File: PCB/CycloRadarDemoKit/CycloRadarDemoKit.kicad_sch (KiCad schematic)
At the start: 13 parts, among them J101 I2C conn, J102 CAN, J103 100BASE-T1, J104 Radar debug, J105 Radar pins, U101 RADAR POGO pins

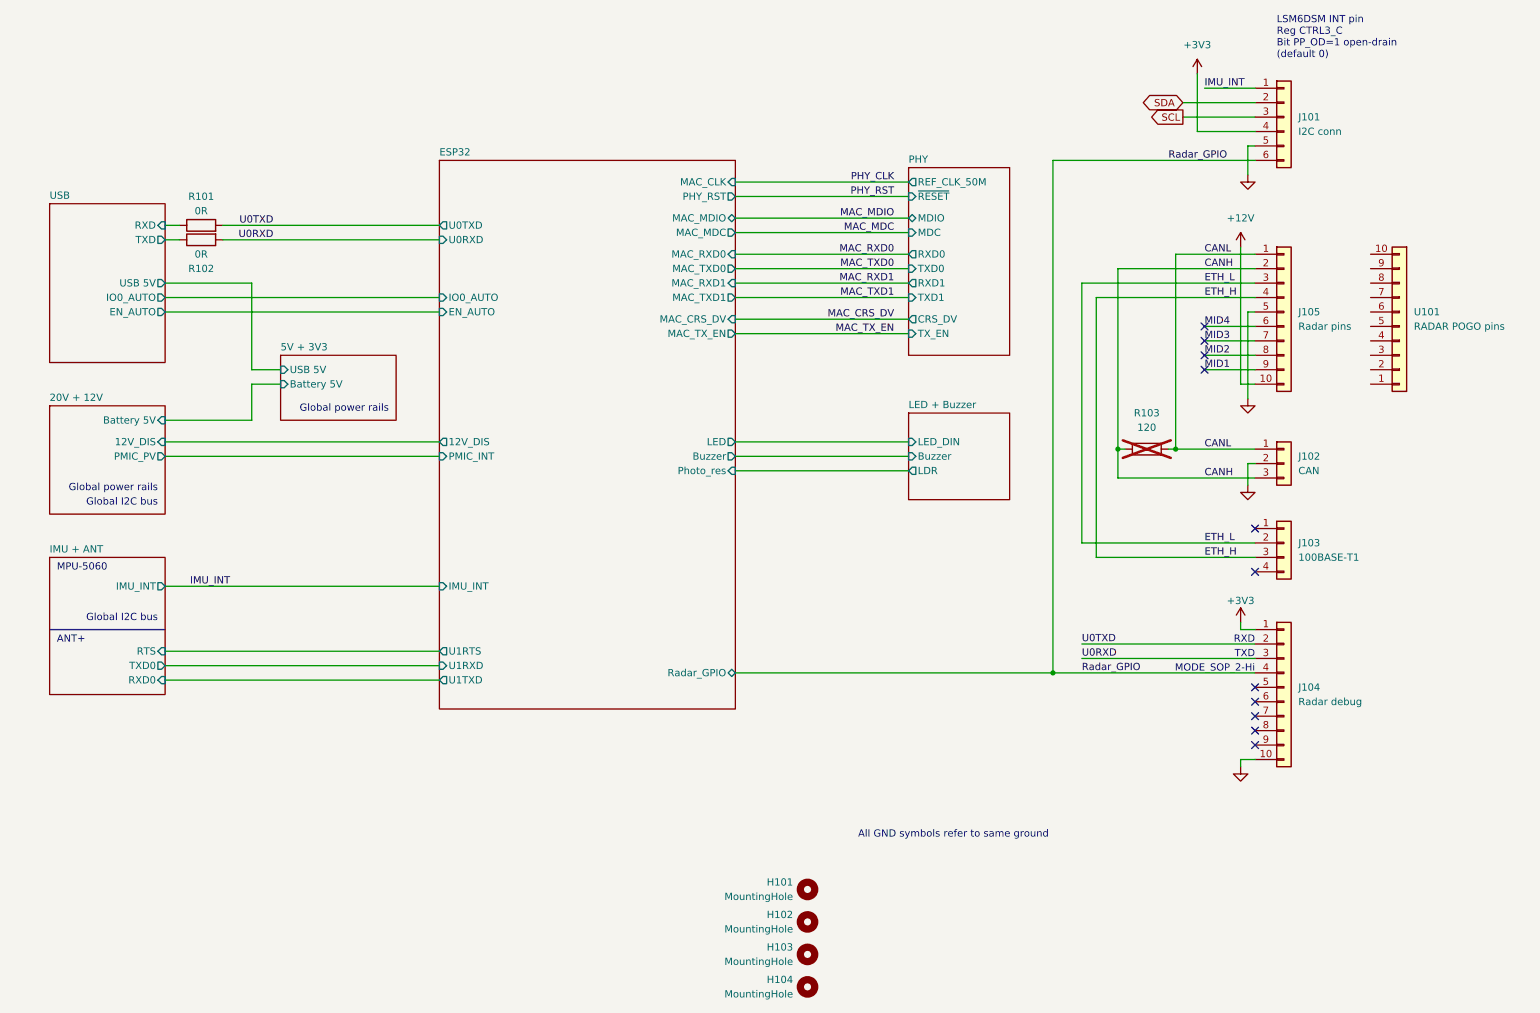
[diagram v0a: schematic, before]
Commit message: reanotated schematic, routing started
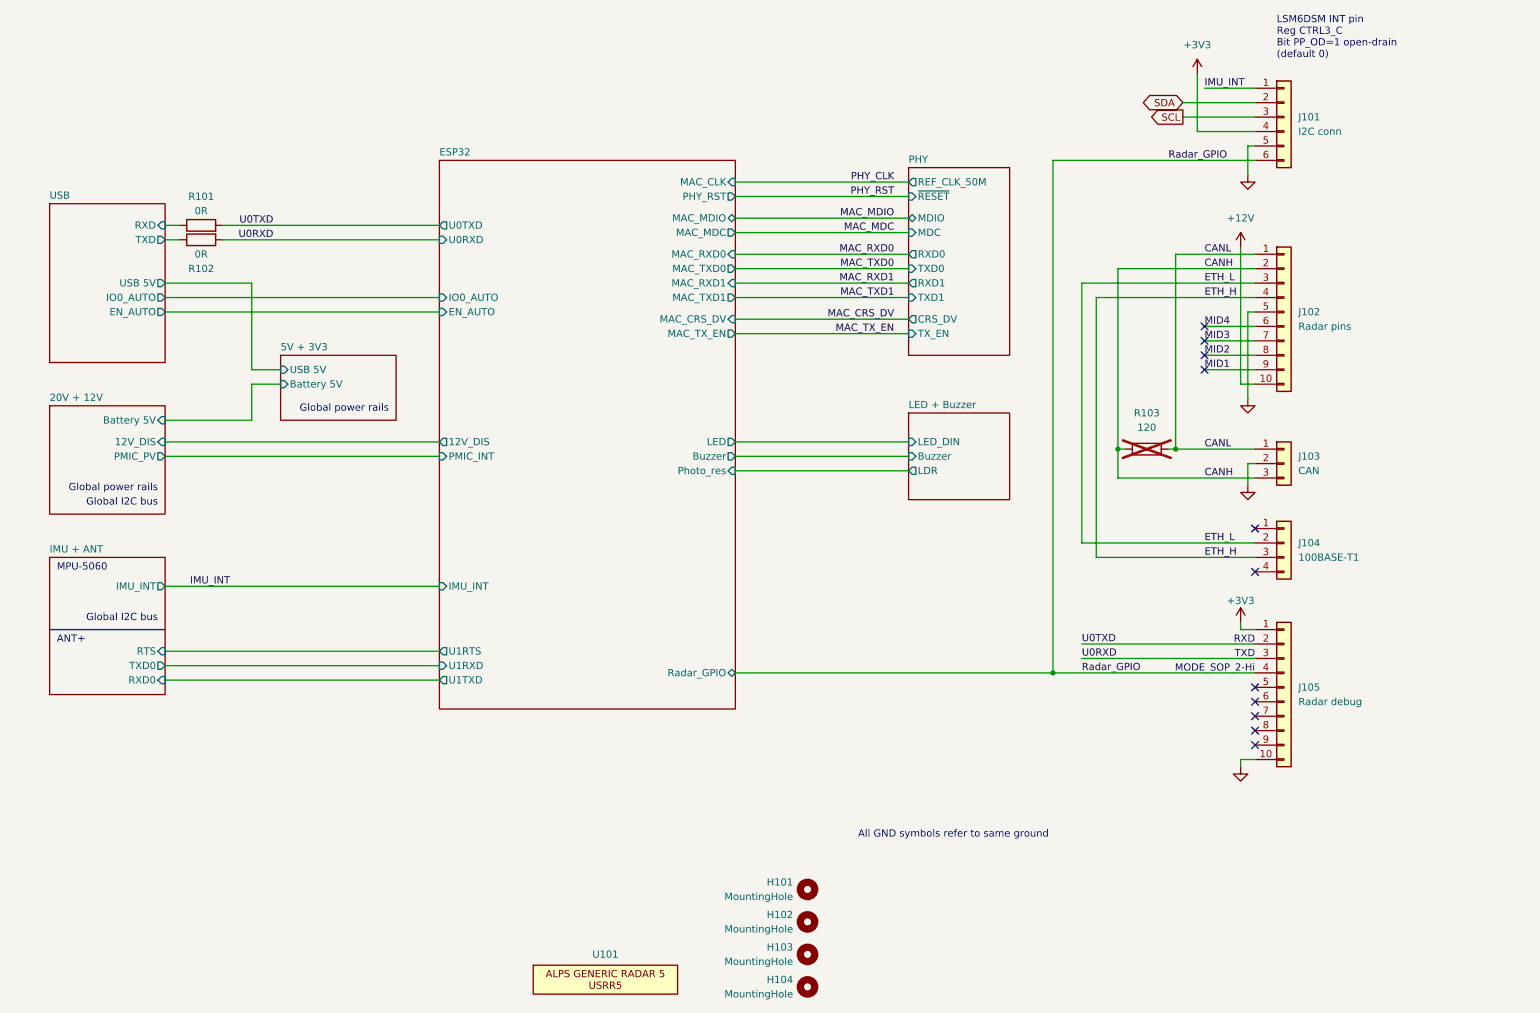
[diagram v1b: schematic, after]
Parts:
- removed U101: RADAR POGO pins, alps_modules:ALPS_USRR5, symbol alps_modules:ALPS_Generic_Radar_5
- added U101: ~, alps_modules:ALPS_USRR5_woPins, symbol alps_modules:ALPS_Generic_Radar_5_block
- renumbered J105 to J102, J102 to J103, J103 to J104, J104 to J105
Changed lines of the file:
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@@
   (symbol (lib_id "Connector_Generic:Conn_01x03") (at 251.46 97.79 0) (unit 1)
     (in_bom yes) (on_board yes) (dnp no) (fields_autoplaced)
-    (property "Reference" "J102" (at 254 96.52 0)
+    (property "Reference" "J103" (at 254 96.52 0)
       (effects (font (size 1.27 1.27)) (justify left))
     )
@@
       (project "CycloRadarDemoKit"
         (path "/c2cd7ca4-4652-4b3d-a3a8-1cfa66cb11e9"
-          (reference "J102") (unit 1)
+          (reference "J103") (unit 1)
         )
       )
@@
   (symbol (lib_id "Connector_Generic:Conn_01x10") (at 251.46 71.12 0) (unit 1)
     (in_bom yes) (on_board yes) (dnp no) (fields_autoplaced)
-    (property "Reference" "J105" (at 254 71.12 0)
+    (property "Reference" "J102" (at 254 71.12 0)
       (effects (font (size 1.27 1.27)) (justify left))
     )
@@
       (project "CycloRadarDemoKit"
         (path "/c2cd7ca4-4652-4b3d-a3a8-1cfa66cb11e9"
-          (reference "J105") (unit 1)
+          (reference "J102") (unit 1)
         )
       )
@@
   (symbol (lib_id "power:GND") (at 245.11 101.6 0) (unit 1)
     (in_bom yes) (on_board yes) (dnp no) (fields_autoplaced)
-    (property "Reference" "#PWR0107" (at 245.11 107.95 0)
+    (property "Reference" "#PWR0105" (at 245.11 107.95 0)
       (effects (font (size 1.27 1.27)) hide)
     )
@@
       (project "CycloRadarDemoKit"
         (path "/c2cd7ca4-4652-4b3d-a3a8-1cfa66cb11e9"
-          (reference "#PWR0107") (unit 1)
-        )
-      )
-    )
-  )
-  (symbol (lib_id "alps_modules:ALPS_Generic_Radar_5") (at 271.78 72.39 180) (unit 1)
-    (in_bom yes) (on_board yes) (dnp no) (fields_autoplaced)
-    (property "Reference" "U101" (at 274.32 71.12 0)
-      (effects (font (size 1.27 1.27)) (justify right))
-    )
-    (property "Value" "RADAR POGO pins" (at 274.32 73.66 0)
-      (effects (font (size 1.27 1.27)) (justify right))
-    )
-    (property "Footprint" "alps_modules:ALPS_USRR5" (at 271.78 72.39 0)
-      (effects (font (size 1.27 1.27)) hide)
-    )
-    (property "Datasheet" "" (at 271.78 72.39 0)
-      (effects (font (size 1.27 1.27)) hide)
-    )
-    (pin "3")
-    (pin "8")
-    (pin "6")
-    (pin "10")
-    (pin "4")
-    (pin "7")
-    (pin "5")
-    (pin "1")
-    (pin "2")
-    (pin "9")
-    (instances
-      (project "CycloRadarDemoKit"
-        (path "/c2cd7ca4-4652-4b3d-a3a8-1cfa66cb11e9"
-          (reference "U101") (unit 1)
+          (reference "#PWR0105") (unit 1)
         )
       )
@@
   (symbol (lib_id "power:+3V3") (at 243.84 125.73 0) (unit 1)
     (in_bom yes) (on_board yes) (dnp no)
-    (property "Reference" "#PWR0105" (at 243.84 129.54 0)
+    (property "Reference" "#PWR0106" (at 243.84 129.54 0)
       (effects (font (size 1.27 1.27)) hide)
     )
@@
       (project "CycloRadarDemoKit"
         (path "/c2cd7ca4-4652-4b3d-a3a8-1cfa66cb11e9"
-          (reference "#PWR0105") (unit 1)
+          (reference "#PWR0106") (unit 1)
         )
       )
@@
   (symbol (lib_id "power:GND") (at 243.84 151.13 0) (unit 1)
     (in_bom yes) (on_board yes) (dnp no) (fields_autoplaced)
-    (property "Reference" "#PWR0106" (at 243.84 157.48 0)
+    (property "Reference" "#PWR0107" (at 243.84 157.48 0)
       (effects (font (size 1.27 1.27)) hide)
     )
@@
       (project "CycloRadarDemoKit"
         (path "/c2cd7ca4-4652-4b3d-a3a8-1cfa66cb11e9"
-          (reference "#PWR0106") (unit 1)
+          (reference "#PWR0107") (unit 1)
+        )
+      )
+    )
+  )
+  (symbol (lib_id "alps_modules:ALPS_Generic_Radar_5_block") (at 132.08 184.785 0) (unit 1)
+    (in_bom yes) (on_board yes) (dnp no) (fields_autoplaced)
+    (property "Reference" "U101" (at 132.08 184.15 0)
+      (effects (font (size 1.27 1.27)))
+    )
+    (property "Value" "~" (at 132.08 184.785 0)
+      (effects (font (size 1.27 1.27)))
+    )
+    (property "Footprint" "alps_modules:ALPS_USRR5_woPins" (at 132.08 184.785 0)
+      (effects (font (size 1.27 1.27)) hide)
+    )
+    (property "Datasheet" "" (at 132.08 184.785 0)
+      (effects (font (size 1.27 1.27)) hide)
+    )
+    (instances
+      (project "CycloRadarDemoKit"
+        (path "/c2cd7ca4-4652-4b3d-a3a8-1cfa66cb11e9"
+          (reference "U101") (unit 1)
         )
       )
@@
     )
   )
-  (symbol (lib_id "Connector_Generic:Conn_01x10") (at 251.46 137.16 0) (unit 1)
-    (in_bom yes) (on_board yes) (dnp no) (fields_autoplaced)
-    (property "Reference" "J104" (at 254 137.16 0)
+  (symbol (lib_name "Conn_01x10_1") (lib_id "Connector_Generic:Conn_01x10") (at 251.46 137.16 0) (unit 1)
+    (in_bom yes) (on_board yes) (dnp no) (fields_autoplaced)
+    (property "Reference" "J105" (at 254 137.16 0)
       (effects (font (size 1.27 1.27)) (justify left))
     )
@@
     (pin "6")
     (pin "1")
-    (instances
-      (project "CycloRadarDemoKit"
-        (path "/c2cd7ca4-4652-4b3d-a3a8-1cfa66cb11e9"
-          (reference "J104") (unit 1)
+    (pin "NC")
+    (instances
+      (project "CycloRadarDemoKit"
+        (path "/c2cd7ca4-4652-4b3d-a3a8-1cfa66cb11e9"
+          (reference "J105") (unit 1)
         )
       )
@@
   (symbol (lib_id "Connector_Generic:Conn_01x04") (at 251.46 111.76 0) (unit 1)
     (in_bom yes) (on_board yes) (dnp no) (fields_autoplaced)
-    (property "Reference" "J103" (at 254 111.76 0)
+    (property "Reference" "J104" (at 254 111.76 0)
       (effects (font (size 1.27 1.27)) (justify left))
     )
@@
       (project "CycloRadarDemoKit"
         (path "/c2cd7ca4-4652-4b3d-a3a8-1cfa66cb11e9"
-          (reference "J103") (unit 1)
-        )
-      )
+          (reference "J104") (unit 1)
+        )
+      )

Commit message: silkscreen repaired
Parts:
- H101, H102, H103, H104: footprint MountingHole:MountingHole_2.7mm_M2.5_ISO7380 -> MountingHole:MountingHole_2.7mm_M2.5_ISO7380_Pad
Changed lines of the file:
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@@
       (effects (font (size 1.27 1.27)) (justify left))
     )
-    (property "Footprint" "MountingHole:MountingHole_2.7mm_M2.5_ISO7380" (at 167.64 178.435 0)
+    (property "Footprint" "MountingHole:MountingHole_2.7mm_M2.5_ISO7380_Pad" (at 167.64 178.435 0)
       (effects (font (size 1.27 1.27)) hide)
     )
@@
       (effects (font (size 1.27 1.27)) (justify left))
     )
-    (property "Footprint" "MountingHole:MountingHole_2.7mm_M2.5_ISO7380" (at 167.64 172.72 0)
+    (property "Footprint" "MountingHole:MountingHole_2.7mm_M2.5_ISO7380_Pad" (at 167.64 172.72 0)
       (effects (font (size 1.27 1.27)) hide)
     )
@@
       (effects (font (size 1.27 1.27)) (justify left))
     )
-    (property "Footprint" "MountingHole:MountingHole_2.7mm_M2.5_ISO7380" (at 167.64 184.15 0)
+    (property "Footprint" "MountingHole:MountingHole_2.7mm_M2.5_ISO7380_Pad" (at 167.64 184.15 0)
       (effects (font (size 1.27 1.27)) hide)
     )
@@
       (effects (font (size 1.27 1.27)) (justify left))
     )
-    (property "Footprint" "MountingHole:MountingHole_2.7mm_M2.5_ISO7380" (at 167.64 189.865 0)
-      (effects (font (size 1.27 1.27)) hide)
-    )
+    (property "Footprint" "MountingHole:MountingHole_2.7mm_M2.5_ISO7380_Pad" (at 167.64 189.865 0)
+      (effects (font (size 1.27 1.27)) hide)
+    )

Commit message: start of repair after review
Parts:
- J102, R103, U101: now left out of the parts list
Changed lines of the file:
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@@
+    (stroke (width 0) (type default))
+  )
+  (wire (pts (xy 218.44 114.3) (xy 246.38 114.3))
     (stroke (width 0) (type default))
   )
@@
     (stroke (width 0) (type default))
   )
-  (wire (pts (xy 215.9 111.76) (xy 246.38 111.76))
-    (stroke (width 0) (type default))
-  )
   (wire (pts (xy 243.84 127) (xy 243.84 125.73))
     (stroke (width 0) (type default))
@@
     (stroke (width 0) (type default))
   )
-  (wire (pts (xy 218.44 114.3) (xy 218.44 68.58))
-    (stroke (width 0) (type default))
-  )
   (wire (pts (xy 233.68 34.29) (xy 246.38 34.29))
     (stroke (width 0) (type default))
@@
     (stroke (width 0) (type default))
   )
-  (wire (pts (xy 215.9 111.76) (xy 215.9 66.04))
+  (wire (pts (xy 215.9 66.04) (xy 215.9 111.76))
     (stroke (width 0) (type default))
   )
@@
   )
   (wire (pts (xy 69.85 83.82) (xy 74.93 83.82))
+    (stroke (width 0) (type default))
+  )
+  (wire (pts (xy 218.44 68.58) (xy 218.44 114.3))
     (stroke (width 0) (type default))
   )
@@
     (stroke (width 0) (type default))
   )
+  (wire (pts (xy 246.38 111.76) (xy 215.9 111.76))
+    (stroke (width 0) (type default))
+  )
   (wire (pts (xy 237.49 76.2) (xy 246.38 76.2))
     (stroke (width 0) (type default))
@@
   )
   (wire (pts (xy 54.61 130.81) (xy 102.87 130.81))
-    (stroke (width 0) (type default))
-  )
-  (wire (pts (xy 218.44 114.3) (xy 246.38 114.3))
     (stroke (width 0) (type default))
   )
@@
   )
   (symbol (lib_id "Connector_Generic:Conn_01x10") (at 251.46 71.12 0) (unit 1)
-    (in_bom yes) (on_board yes) (dnp no) (fields_autoplaced)
+    (in_bom no) (on_board yes) (dnp no) (fields_autoplaced)
     (property "Reference" "J102" (at 254 71.12 0)
       (effects (font (size 1.27 1.27)) (justify left))
@@
   )
   (symbol (lib_id "alps_modules:ALPS_Generic_Radar_5_block") (at 132.08 184.785 0) (unit 1)
-    (in_bom yes) (on_board yes) (dnp no) (fields_autoplaced)
+    (in_bom no) (on_board yes) (dnp no) (fields_autoplaced)
     (property "Reference" "U101" (at 132.08 184.15 0)
       (effects (font (size 1.27 1.27)))
@@
   )
   (symbol (lib_id "Device:R") (at 227.33 95.25 90) (unit 1)
-    (in_bom yes) (on_board yes) (dnp yes) (fields_autoplaced)
+    (in_bom no) (on_board yes) (dnp yes) (fields_autoplaced)
     (property "Reference" "R103" (at 227.33 88.9 90)
       (effects (font (size 1.27 1.27)))

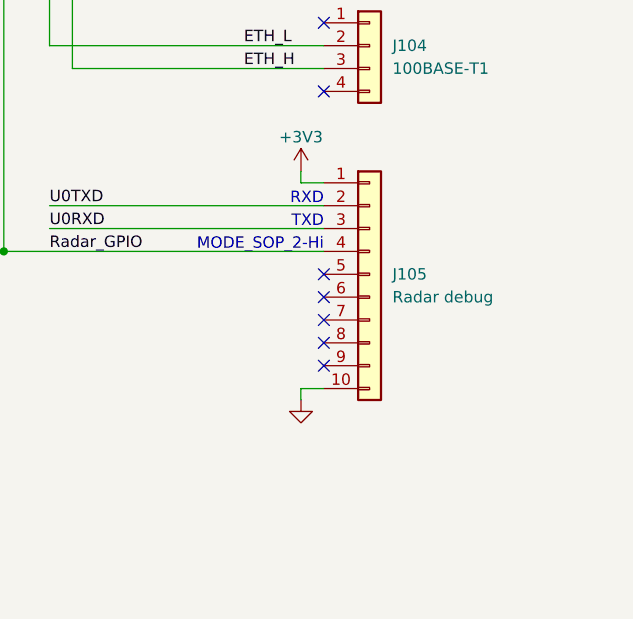
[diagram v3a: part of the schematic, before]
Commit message: Review changes WIP, USB ESD changed, MDIC pullup added
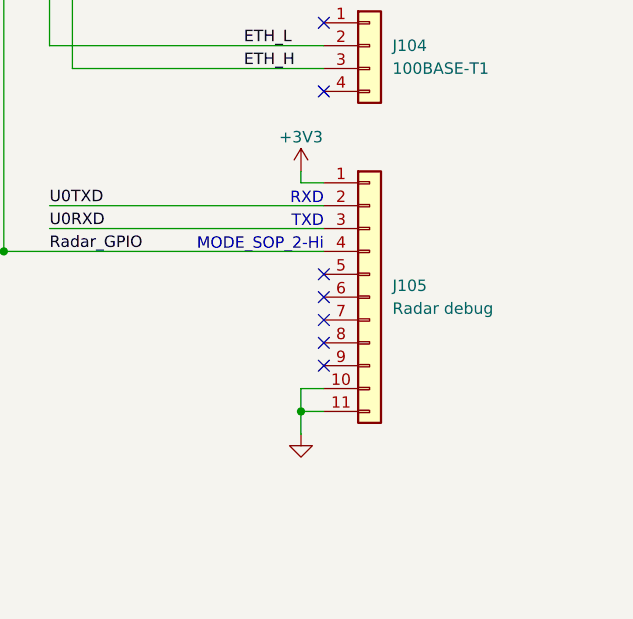
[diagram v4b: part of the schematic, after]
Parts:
- J105: symbol Connector_Generic:Conn_01x10 -> Connector_Generic:Conn_01x11
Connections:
- net GND: now also J105.11 (Pin_11)
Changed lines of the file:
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@@
   (junction (at 232.41 95.25) (diameter 0) (color 0 0 0 0)
+  )
+  (junction (at 243.84 152.4) (diameter 0) (color 0 0 0 0)
   )
   (junction (at 222.25 95.25) (diameter 0) (color 0 0 0 0)
@@
     (stroke (width 0) (type default))
   )
-  (wire (pts (xy 243.84 149.86) (xy 243.84 151.13))
+  (wire (pts (xy 243.84 149.86) (xy 243.84 152.4))
     (stroke (width 0) (type default))
   )
@@
   )
   (wire (pts (xy 222.25 63.5) (xy 246.38 63.5))
+    (stroke (width 0) (type default))
+  )
+  (wire (pts (xy 243.84 152.4) (xy 246.38 152.4))
     (stroke (width 0) (type default))
   )
@@
   (polyline (pts (xy 54.61 127) (xy 35.56 127))
     (stroke (width 0) (type default) (color 153 0 0 1))
+  )
+  (wire (pts (xy 243.84 152.4) (xy 243.84 154.94))
+    (stroke (width 0) (type default))
   )
   (wire (pts (xy 246.38 127) (xy 243.84 127))
@@
     )
   )
-  (symbol (lib_id "power:GND") (at 243.84 151.13 0) (unit 1)
+  (symbol (lib_id "power:GND") (at 243.84 154.94 0) (unit 1)
     (in_bom yes) (on_board yes) (dnp no) (fields_autoplaced)
-    (property "Reference" "#PWR0107" (at 243.84 157.48 0)
-      (effects (font (size 1.27 1.27)) hide)
-    )
-    (property "Value" "GND" (at 243.84 156.21 0)
-      (effects (font (size 1.27 1.27)) hide)
-    )
-    (property "Footprint" "" (at 243.84 151.13 0)
-      (effects (font (size 1.27 1.27)) hide)
-    )
-    (property "Datasheet" "" (at 243.84 151.13 0)
+    (property "Reference" "#PWR0107" (at 243.84 161.29 0)
+      (effects (font (size 1.27 1.27)) hide)
+    )
+    (property "Value" "GND" (at 243.84 160.02 0)
+      (effects (font (size 1.27 1.27)) hide)
+    )
+    (property "Footprint" "" (at 243.84 154.94 0)
+      (effects (font (size 1.27 1.27)) hide)
+    )
+    (property "Datasheet" "" (at 243.84 154.94 0)
       (effects (font (size 1.27 1.27)) hide)
     )
@@
     )
   )
-  (symbol (lib_name "Conn_01x10_1") (lib_id "Connector_Generic:Conn_01x10") (at 251.46 137.16 0) (unit 1)
+  (symbol (lib_id "Connector_Generic:Conn_01x11") (at 251.46 139.7 0) (unit 1)
     (in_bom yes) (on_board yes) (dnp no) (fields_autoplaced)
-    (property "Reference" "J105" (at 254 137.16 0)
-      (effects (font (size 1.27 1.27)) (justify left))
-    )
-    (property "Value" "Radar debug" (at 254 139.7 0)
-      (effects (font (size 1.27 1.27)) (justify left))
-    )
-    (property "Footprint" "Connector_FFC-FPC:AFC30-S10FCC-00" (at 251.46 137.16 0)
-      (effects (font (size 1.27 1.27)) hide)
-    )
-    (property "Datasheet" "https://datasheet.lcsc.com/lcsc/2304140030_JUSHUO-AFC30-S10FCC-00_C395235.pdf" (at 251.46 137.16 0)
-      (effects (font (size 1.27 1.27)) hide)
-    )
-    (property "LCSC" "C395235" (at 251.46 137.16 0)
+    (property "Reference" "J105" (at 254 138.43 0)
+      (effects (font (size 1.27 1.27)) (justify left))
+    )
+    (property "Value" "Radar debug" (at 254 140.97 0)
+      (effects (font (size 1.27 1.27)) (justify left))
+    )
+    (property "Footprint" "Connector_FFC-FPC:AFC30-S10FCC-00" (at 251.46 139.7 0)
+      (effects (font (size 1.27 1.27)) hide)
+    )
+    (property "Datasheet" "~" (at 251.46 139.7 0)
+      (effects (font (size 1.27 1.27)) hide)
+    )
+    (property "LCSC" "C395235" (at 251.46 139.7 0)
       (effects (font (size 1.27 1.27)) hide)
     )
@@
     (pin "6")
     (pin "1")
-    (pin "NC")
-    (instances
-      (project "CycloRadarDemoKit"
+    (pin "11")
+    (instances
+      (project "CycloRadarDemoKit"

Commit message: PCB finished and reviewed
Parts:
- H101, H102, H103, H104: symbol Mechanical:MountingHole -> Mechanical:MountingHole_Pad; now in the parts list
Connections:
- net GND: now also H101.1, H102.1, H103.1, H104.1
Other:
- moved on the sheet: U101
